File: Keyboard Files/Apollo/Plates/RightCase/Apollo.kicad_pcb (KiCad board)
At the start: 2 copper layers, 166.1 x 133.7 mm, 37 parts

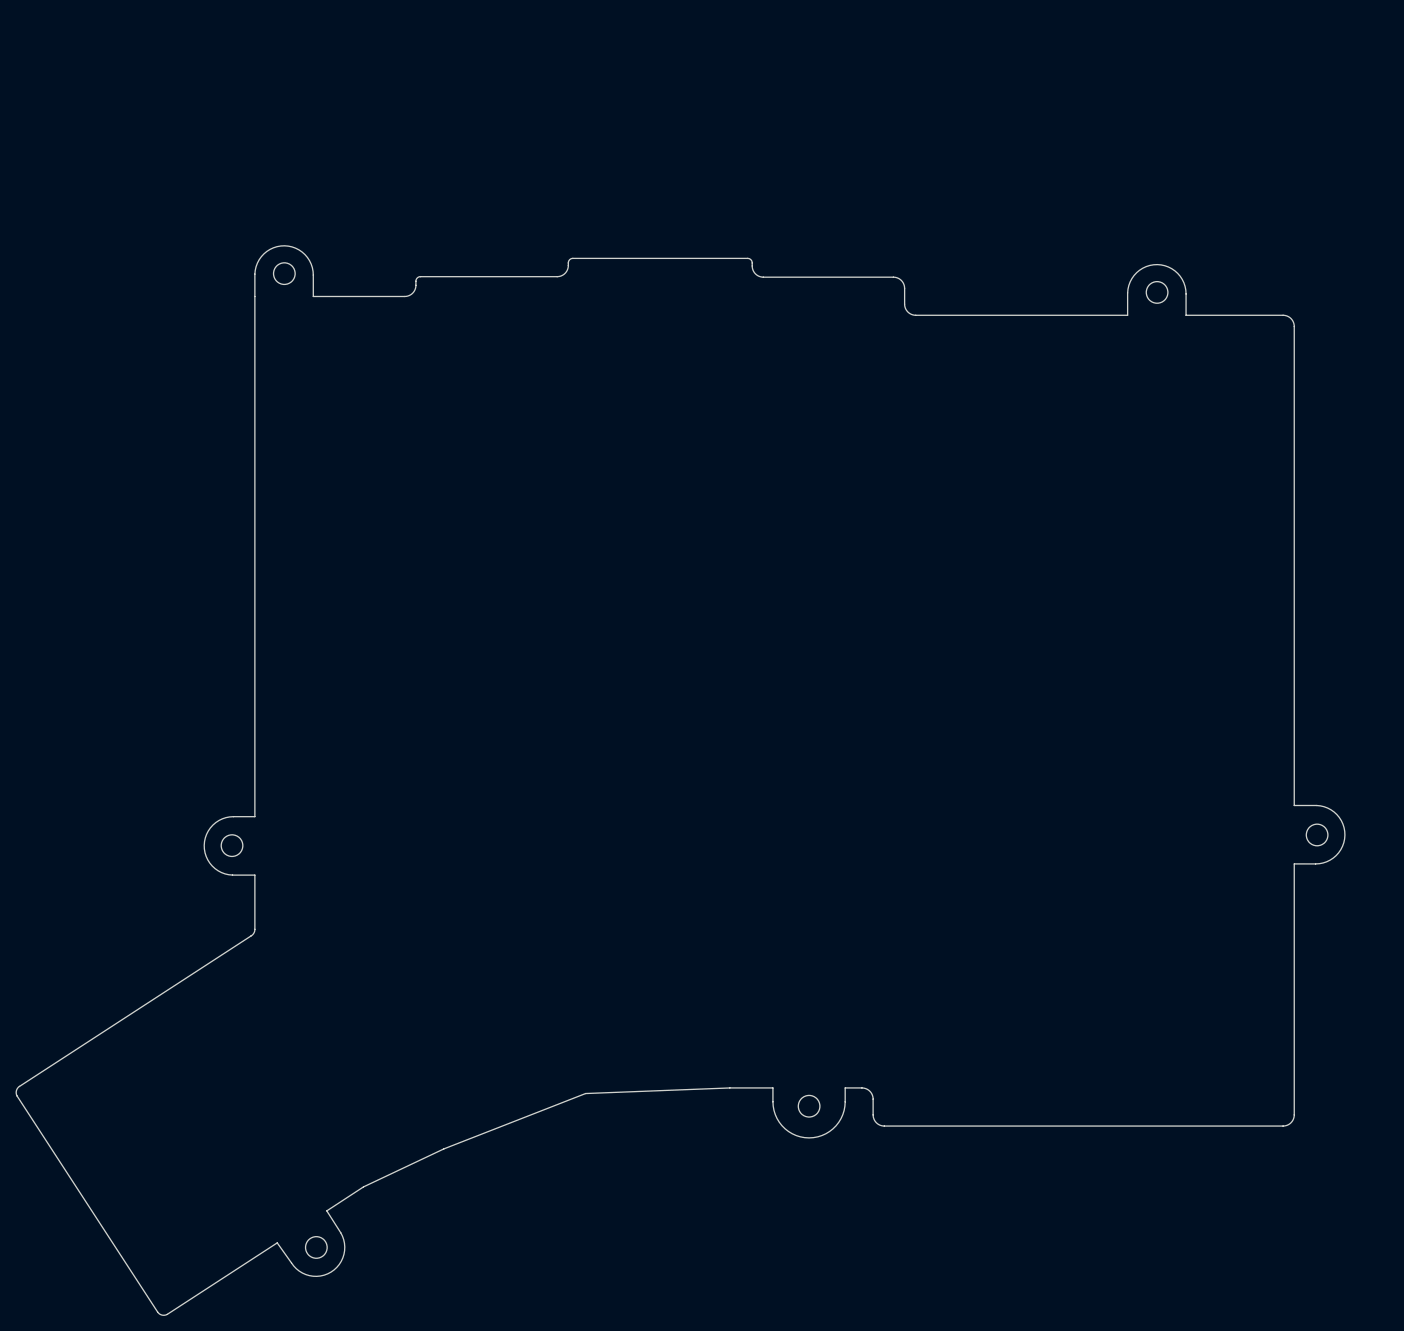
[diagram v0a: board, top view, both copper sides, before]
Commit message: Redo thumb keys plates
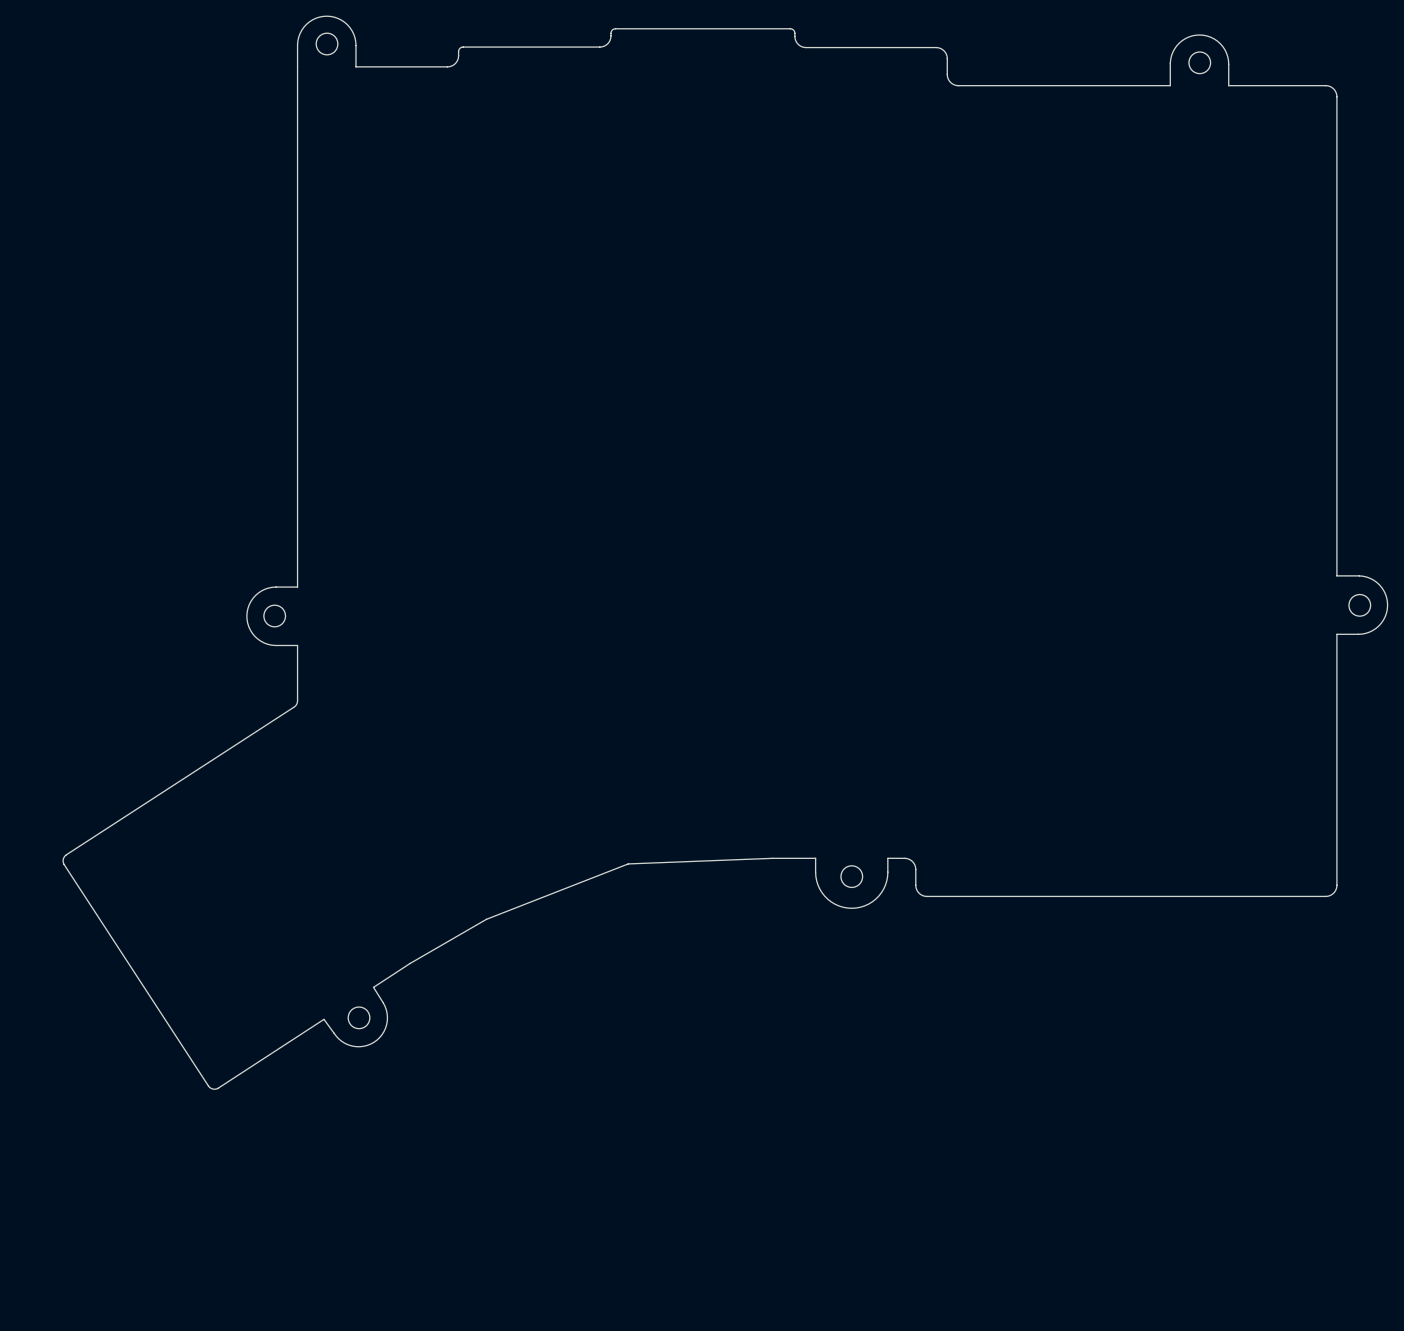
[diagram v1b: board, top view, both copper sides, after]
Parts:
- removed the REF** at (103.9, 154.9)
- removed the REF** at (97.2, 193.0)
- removed the REF** at (113.1, 182.7)
- removed the REF** at (136.5, 175.1)
- removed the REF** at (119.3, 156.0)
- removed the REF** at (119.3, 137.0)
- removed the REF** at (119.3, 117.9)
- removed the REF** at (110.4, 83.4)
- removed the REF** at (138.4, 153.6)
- removed the REF** at (138.4, 134.6)
- removed the REF** at (138.4, 96.5)
- removed the REF** at (138.4, 115.5)
- removed the REF** at (157.4, 94.1)
- removed the REF** at (157.4, 113.2)
- removed the REF** at (157.4, 151.3)
- removed the REF** at (157.4, 132.2)
- removed the REF** at (195.5, 101.2)
- removed the REF** at (219.5, 85.8)
- removed the REF** at (195.5, 120.3)
- removed the REF** at (195.5, 158.4)
- removed the REF** at (195.5, 139.3)
- removed the REF** at (114.4, 205.2)
- removed the REF** at (176.0, 187.5)
- removed the REF** at (119.3, 98.9)
- added REF**: MountingHole_2.7mm_M2.5, MountingHole:MountingHole_2.7mm_M2.5, B.Cu at (109.2, 126.2)
- added REF**: MX_Switch_Cutout, Keebio-Parts:MX_Switch_Cutout, B.Cu at (102.5, 164.3)
- added REF**: MX_Switch_Cutout, Keebio-Parts:MX_Switch_Cutout, B.Cu at (118.4, 154.0)
- added REF**: MX_Switch_Cutout, Keebio-Parts:MX_Switch_Cutout, B.Cu at (141.8, 146.4)
- added REF**: MX_Switch_Cutout, Keebio-Parts:MX_Switch_Cutout, B.Cu at (124.7, 127.3)
- added REF**: MX_Switch_Cutout, Keebio-Parts:MX_Switch_Cutout, B.Cu at (124.7, 108.3)
- added REF**: MX_Switch_Cutout, Keebio-Parts:MX_Switch_Cutout, B.Cu at (124.7, 89.2)
- added REF**: MountingHole_2.7mm_M2.5, MountingHole:MountingHole_2.7mm_M2.5, B.Cu at (115.8, 54.7)
- added REF**: MX_Switch_Cutout, Keebio-Parts:MX_Switch_Cutout, B.Cu at (143.7, 124.9)
- added REF**: MX_Switch_Cutout, Keebio-Parts:MX_Switch_Cutout, B.Cu at (143.7, 105.9)
- added REF**: MX_Switch_Cutout, Keebio-Parts:MX_Switch_Cutout, B.Cu at (143.7, 67.8)
- added REF**: MX_Switch_Cutout, Keebio-Parts:MX_Switch_Cutout, B.Cu at (143.7, 86.8)
- added REF**: MX_Switch_Cutout, Keebio-Parts:MX_Switch_Cutout, B.Cu at (162.8, 65.4)
- added REF**: MX_Switch_Cutout, Keebio-Parts:MX_Switch_Cutout, B.Cu at (162.8, 84.5)
- added REF**: MX_Switch_Cutout, Keebio-Parts:MX_Switch_Cutout, B.Cu at (162.8, 122.6)
- added REF**: MX_Switch_Cutout, Keebio-Parts:MX_Switch_Cutout, B.Cu at (162.8, 103.5)
- added REF**: MX_Switch_Cutout, Keebio-Parts:MX_Switch_Cutout, B.Cu at (200.9, 72.5)
- added REF**: MountingHole_2.7mm_M2.5, MountingHole:MountingHole_2.7mm_M2.5, B.Cu at (224.9, 57.1)
- added REF**: MX_Switch_Cutout, Keebio-Parts:MX_Switch_Cutout, B.Cu at (200.9, 91.6)
- added REF**: MX_Switch_Cutout, Keebio-Parts:MX_Switch_Cutout, B.Cu at (200.9, 129.7)
- added REF**: MX_Switch_Cutout, Keebio-Parts:MX_Switch_Cutout, B.Cu at (200.9, 110.6)
- added REF**: MountingHole_2.7mm_M2.5, MountingHole:MountingHole_2.7mm_M2.5, B.Cu at (119.8, 176.5)
- added REF**: MountingHole_2.7mm_M2.5, MountingHole:MountingHole_2.7mm_M2.5, B.Cu at (181.4, 158.8)
- added REF**: MX_Switch_Cutout, Keebio-Parts:MX_Switch_Cutout, B.Cu at (124.7, 70.2)
- moved REF** 29.2 mm to (224.7, 91.6)
- moved REF** 29.2 mm to (181.8, 124.9)
- moved REF** 29.2 mm to (244.9, 124.9)
- moved REF** 29.2 mm to (181.8, 67.8)
- moved REF** 29.2 mm to (224.7, 129.7)
- moved REF** 29.2 mm to (224.7, 72.5)
- moved REF** 29.2 mm to (224.7, 148.7)
- moved REF** 29.2 mm to (162.8, 141.6)
- moved REF** 29.2 mm to (200.9, 148.7)
- moved REF** 29.2 mm to (181.8, 144.0)
- moved REF** 29.2 mm to (181.8, 105.9)
- moved REF** 29.2 mm to (181.8, 86.8)
- moved REF** 29.2 mm to (224.7, 110.6)
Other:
- board size 166.1 x 133.7 mm -> 165.6 x 134.1 mm
